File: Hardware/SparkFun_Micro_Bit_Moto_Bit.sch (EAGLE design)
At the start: 59 parts, among them J1 POWER_JACKPTH_LOCK, J10 Qwiic, J2 CORTEX_JTAG_DEBUG, U1 CY8C4245LQI-483, U2 TPS62172, U3 micro:bit, U4 DRV8835

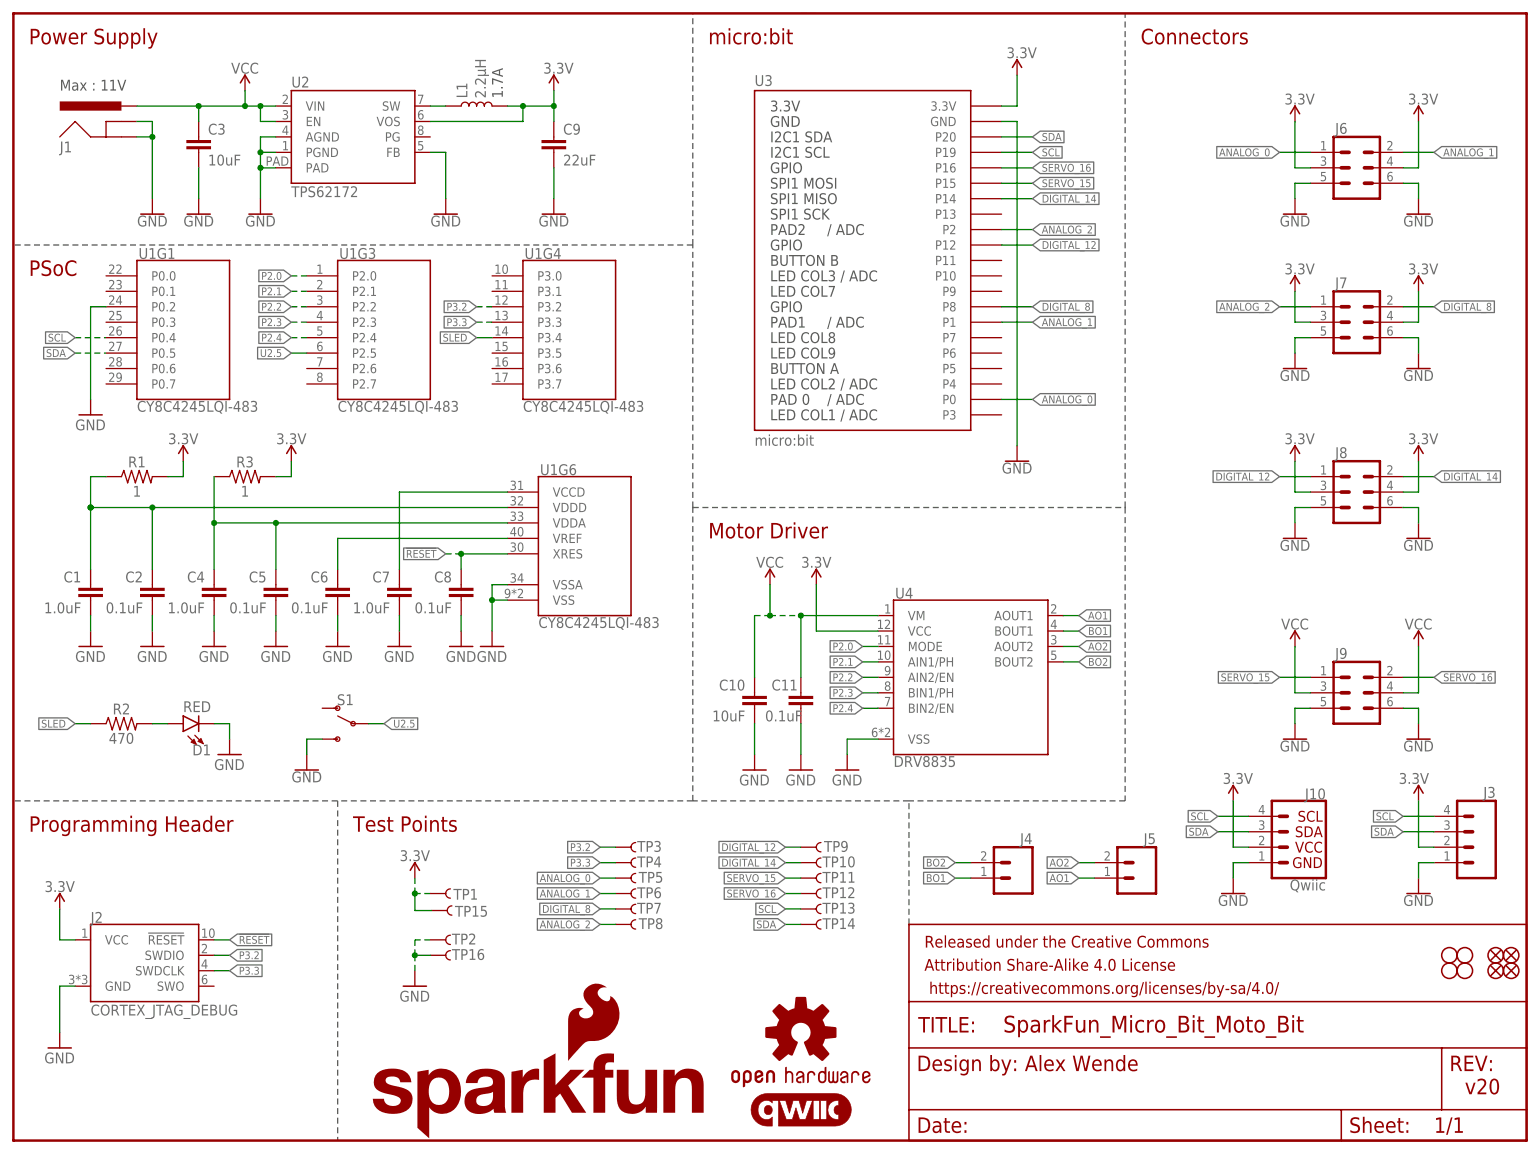
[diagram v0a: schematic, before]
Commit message: v21
- Replaced S1 with new switch
- Added 4.7k pull up resistors for I2C data out
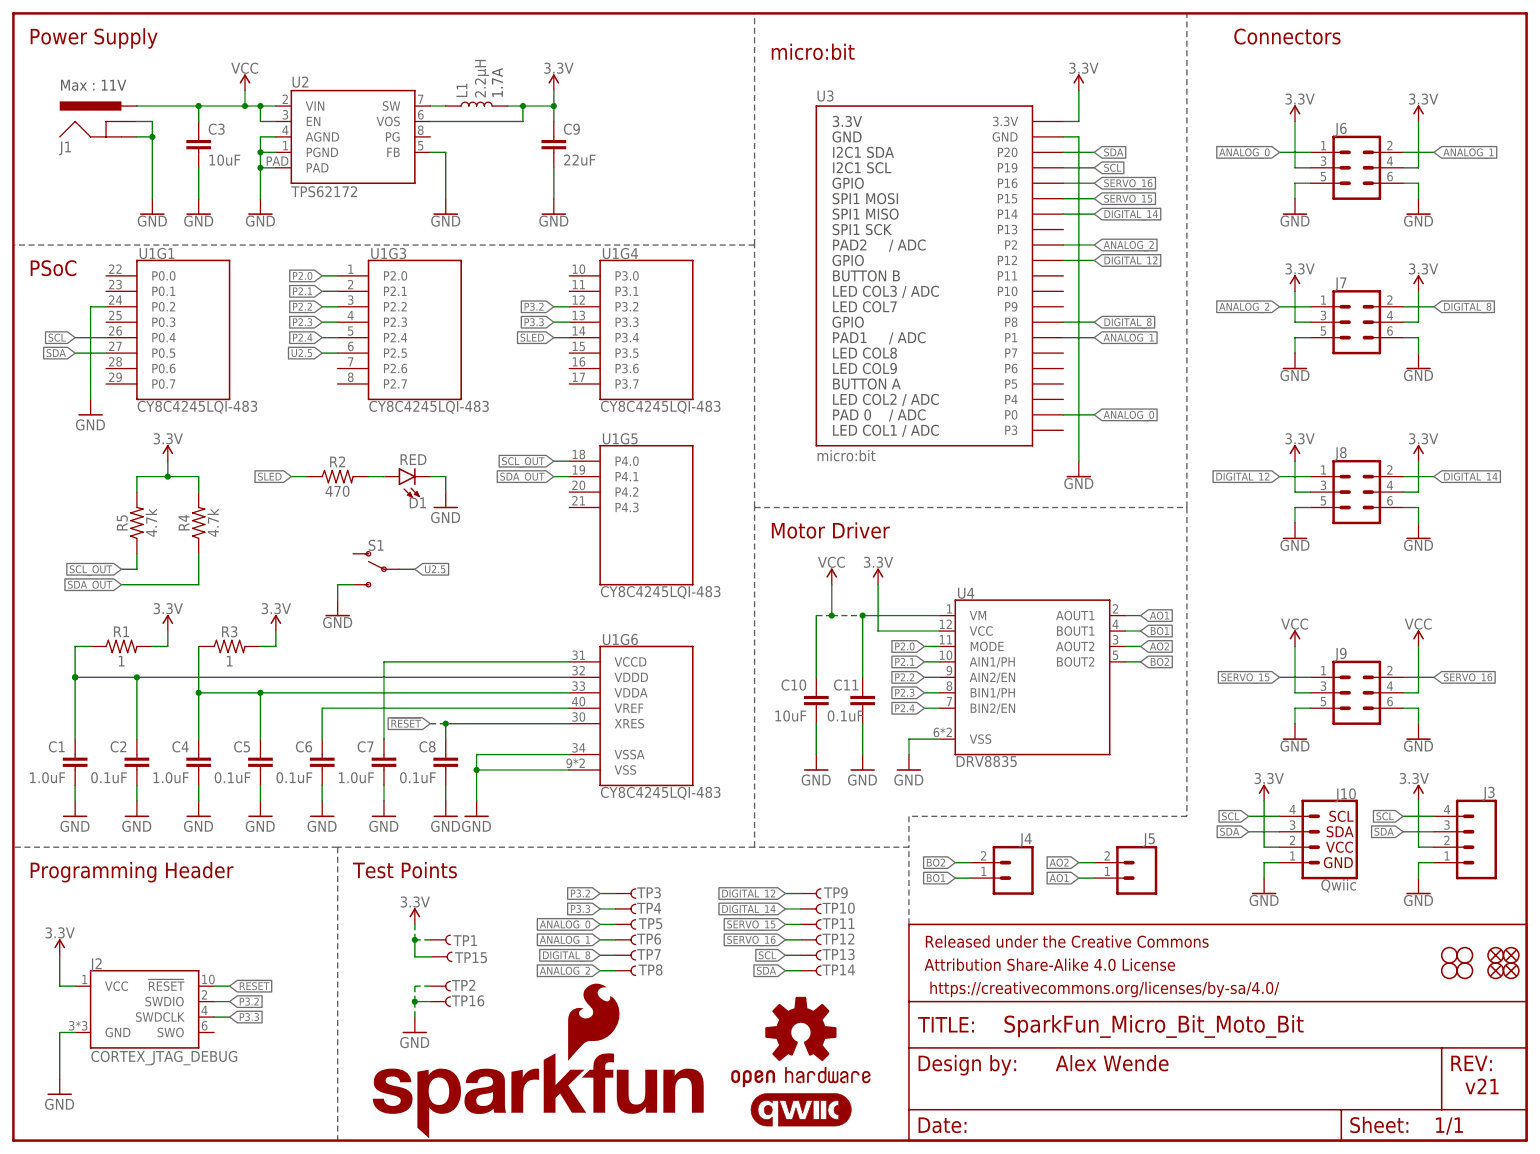
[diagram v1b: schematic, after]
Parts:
- added R4, R5: 4.7k, SparkFun-Resistors:4.7KOHM-0603-1/10W-1%
- S1: device SparkFun-Switches:SWITCH-SPDT-PTH-11.6X4.0MM-SHORT_LEADS -> SparkFun-Switches:SWITCH-SPDT-PTH-8.6X4.3MM-LOCK
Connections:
- new net SCL_OUT: R5.1, U1G5.P4.0
- new net SDA_OUT: R4.1, U1G5.P4.1
- net 3.3V: now also R4.2, R5.2
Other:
- note added: "v21"
- note removed: "v20"
- moved on the sheet: C1, C10, C11, C2, C4, C5, C6, C7, C8, D1, J10, J2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
